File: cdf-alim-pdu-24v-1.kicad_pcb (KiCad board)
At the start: 2 copper layers, 80 x 60 mm, 130 parts, among them J1 Conn_01x02, J10 Conn_01x02, J11 Conn_01x02, J12 Conn_01x02, J13 Conn_01x02, J14 Conn_01x02, J15 Conn_01x02, J16 Conn_01x02, J17 Conn_01x02, J2 Conn_01x02, J3 Conn_01x02, J4 Conn_01x02, J5 Conn_01x02, J6 Conn_01x02, J7 Conn_01x02, J8 Conn_01x02, J9 Conn_01x02, Q1 BSC019N04LS, Q2 BSC019N04LS, Q3 BSC019N04LS, U1 TPS25983, U2 TPS25983, U3 TPS25983, U4 HT753-1, U5 MX25947, U6 MX25947, U7 MX25947

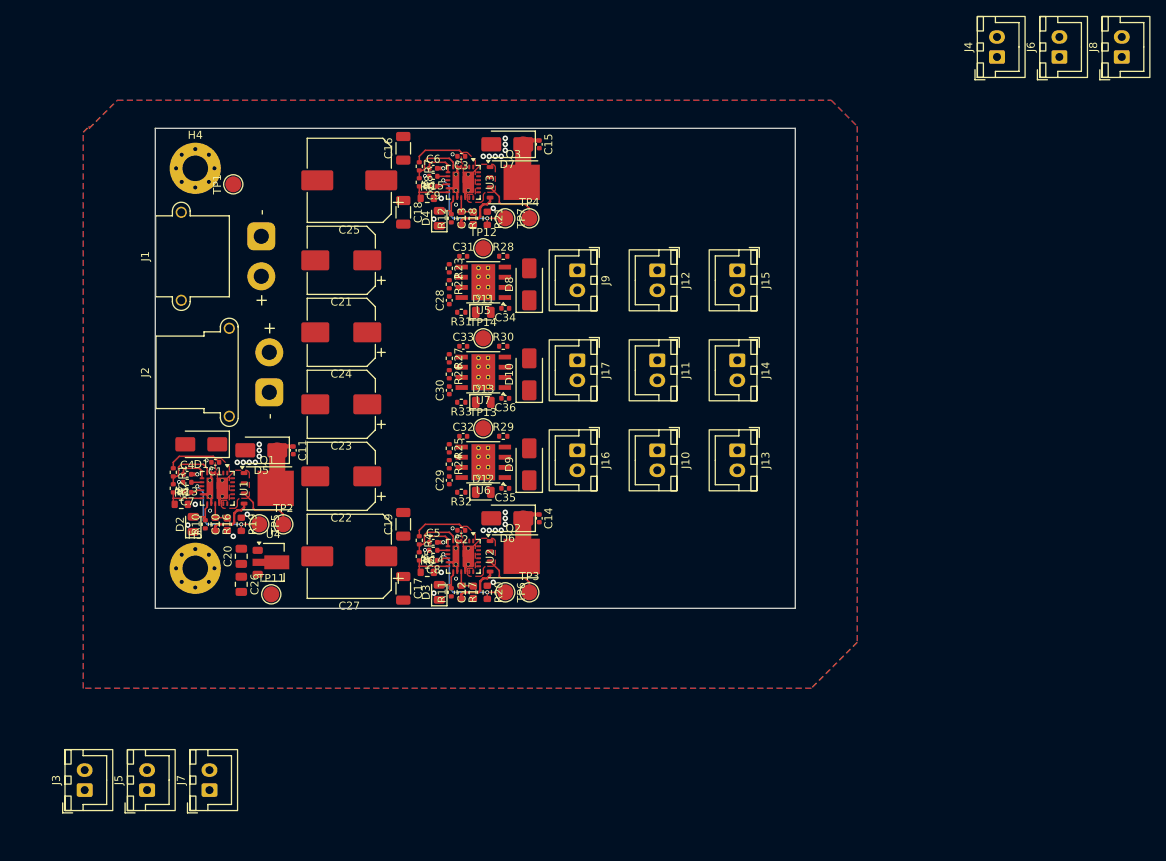
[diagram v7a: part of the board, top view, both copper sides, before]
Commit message: pcb: place all power connectors
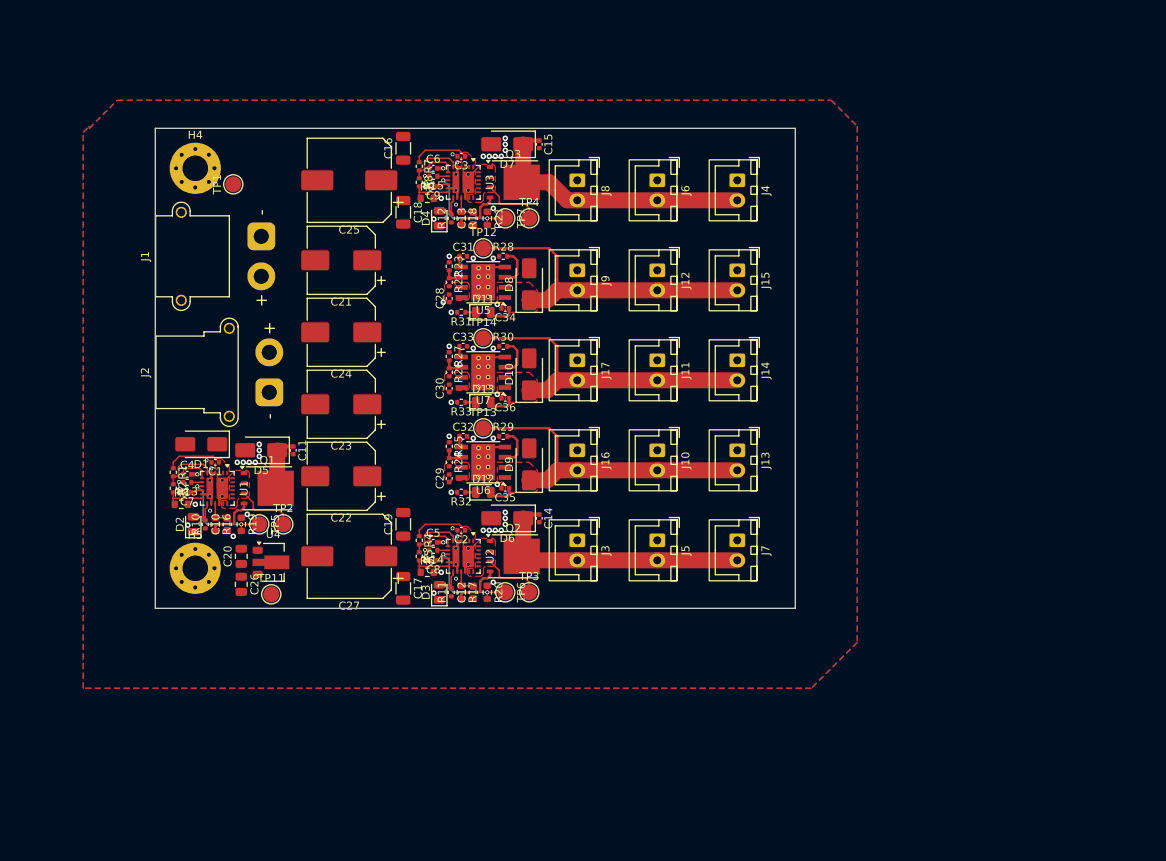
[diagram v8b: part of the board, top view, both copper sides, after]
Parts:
- moved J7 73.0 mm to (232.8, 131.5), turned to -90 degrees
- moved J5 71.0 mm to (222.8, 131.5), turned to -90 degrees
- moved J8 69.8 mm to (212.8, 86.5), turned to -90 degrees
- moved J3 69.0 mm to (212.8, 131.5), turned to -90 degrees
- moved J6 52.6 mm to (222.8, 86.5), turned to -90 degrees
- moved J4 35.9 mm to (232.8, 86.5), turned to -90 degrees
- moved C28 0.25 mm to (196.8, 101.2)
- moved C29 0.25 mm to (196.8, 123.8)
- moved C30 0.25 mm to (196.8, 112.5)
- moved R22 0.25 mm to (196.8, 99.2)
- moved R23 0.25 mm to (196.8, 97.2)
- moved R24 0.25 mm to (196.8, 121.7)
- moved R25 0.25 mm to (196.8, 119.8)
- moved R26 0.25 mm to (196.8, 110.5)
- moved R27 0.25 mm to (196.8, 108.5)
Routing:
- net Net-(D12-A): track 0.00 -> 43.8 mm
- net Net-(D11-A): track 0.00 -> 43.8 mm
- net Net-(D10-K): track 0.00 -> 43.8 mm
- net Net-(D7-K): track 7.03 -> 34.9 mm
- net Net-(D6-K): track 7.03 -> 34.2 mm
- net GND: track 12.8 -> 19.2 mm, vias 49 -> 65
- net Net-(U7-ILIMIT): track 0.00 -> 4.90 mm
- net Net-(U6-ILIMIT): track 0.00 -> 4.90 mm
- net Net-(U5-ILIMIT): track 0.00 -> 4.90 mm
- net Net-(U7-EN/UVLO): track 0.00 -> 2.57 mm
- net Net-(U6-EN/UVLO): track 0.00 -> 2.57 mm
- net Net-(U5-EN/UVLO): track 0.00 -> 2.57 mm
- net Net-(U7-DVDT): track 0.00 -> 1.46 mm
- net Net-(U6-DVDT): track 0.00 -> 1.46 mm
- net Net-(U5-DVDT): track 0.00 -> 1.46 mm
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- added copper zone on F.Cu, net Net-(D10-K)
- added copper zone on F.Cu, net Net-(D11-A)
- added copper zone on F.Cu, net Net-(D12-A)
